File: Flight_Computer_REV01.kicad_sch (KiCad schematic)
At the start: 24 parts, among them J1 Conn_02x03_Counter_Clockwise, J10 Conn_02x16_Top_Bottom, J13 Conn_02x03_Counter_Clockwise, J14 MTR_Signals, J15 Conn_02x30_Odd_Even, J2 Conn_02x03_Counter_Clockwise, J3 AMB POWER, J4 INPUT POWER PASSTHROUGH, J5 Conn_02x16_Top_Bottom, J6 Conn_02x16_Top_Bottom, J7 Conn_02x10_Odd_Even, J8 Conn_02x05_Odd_Even, J9 Conn_02x16_Top_Bottom

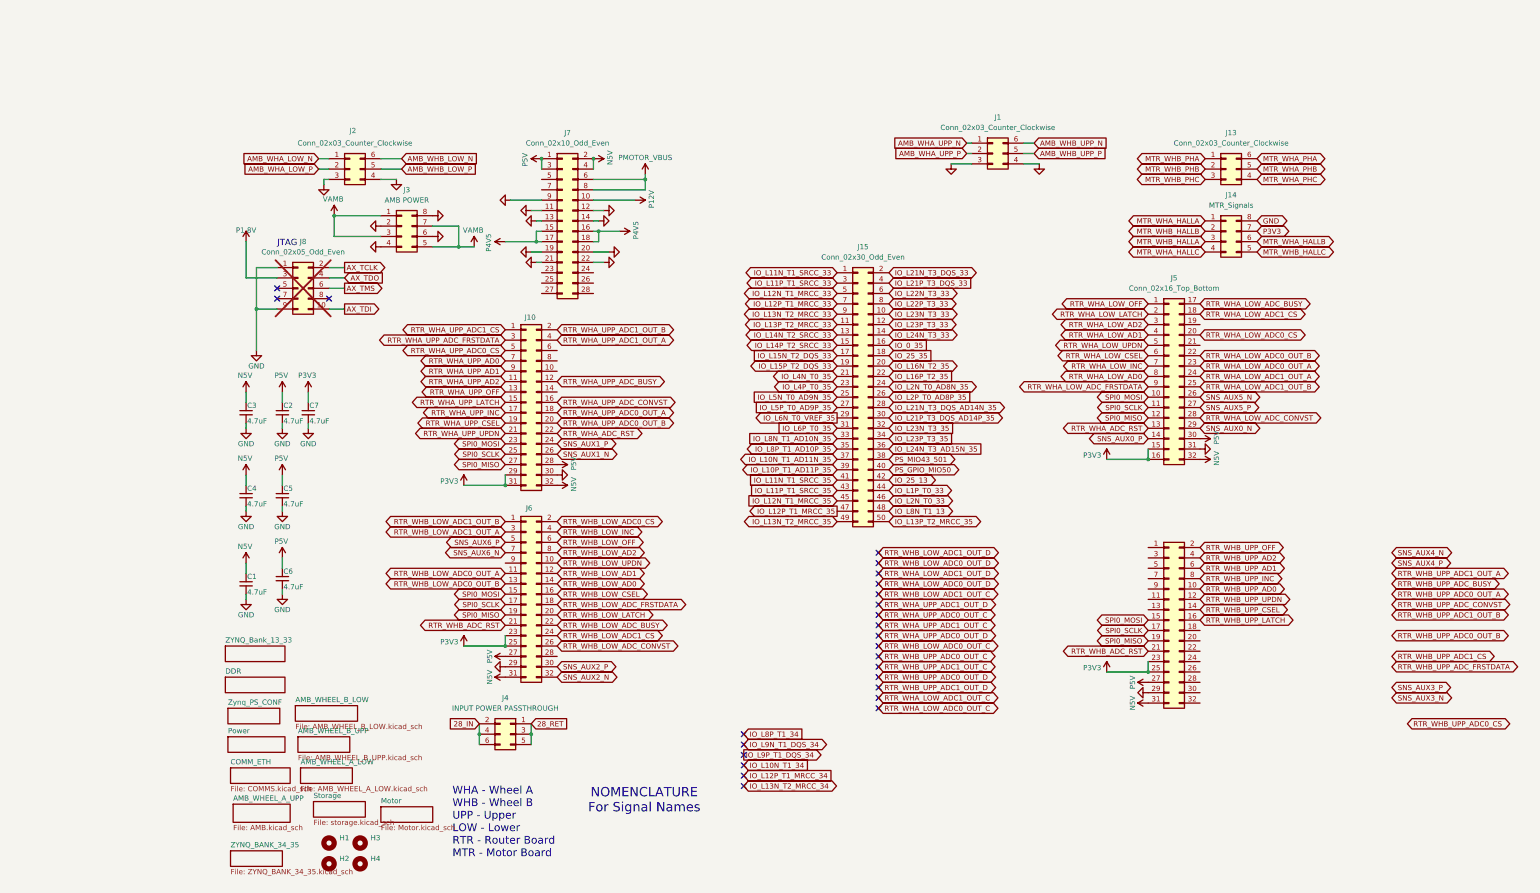
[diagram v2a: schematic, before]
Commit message: Changes to layout pins
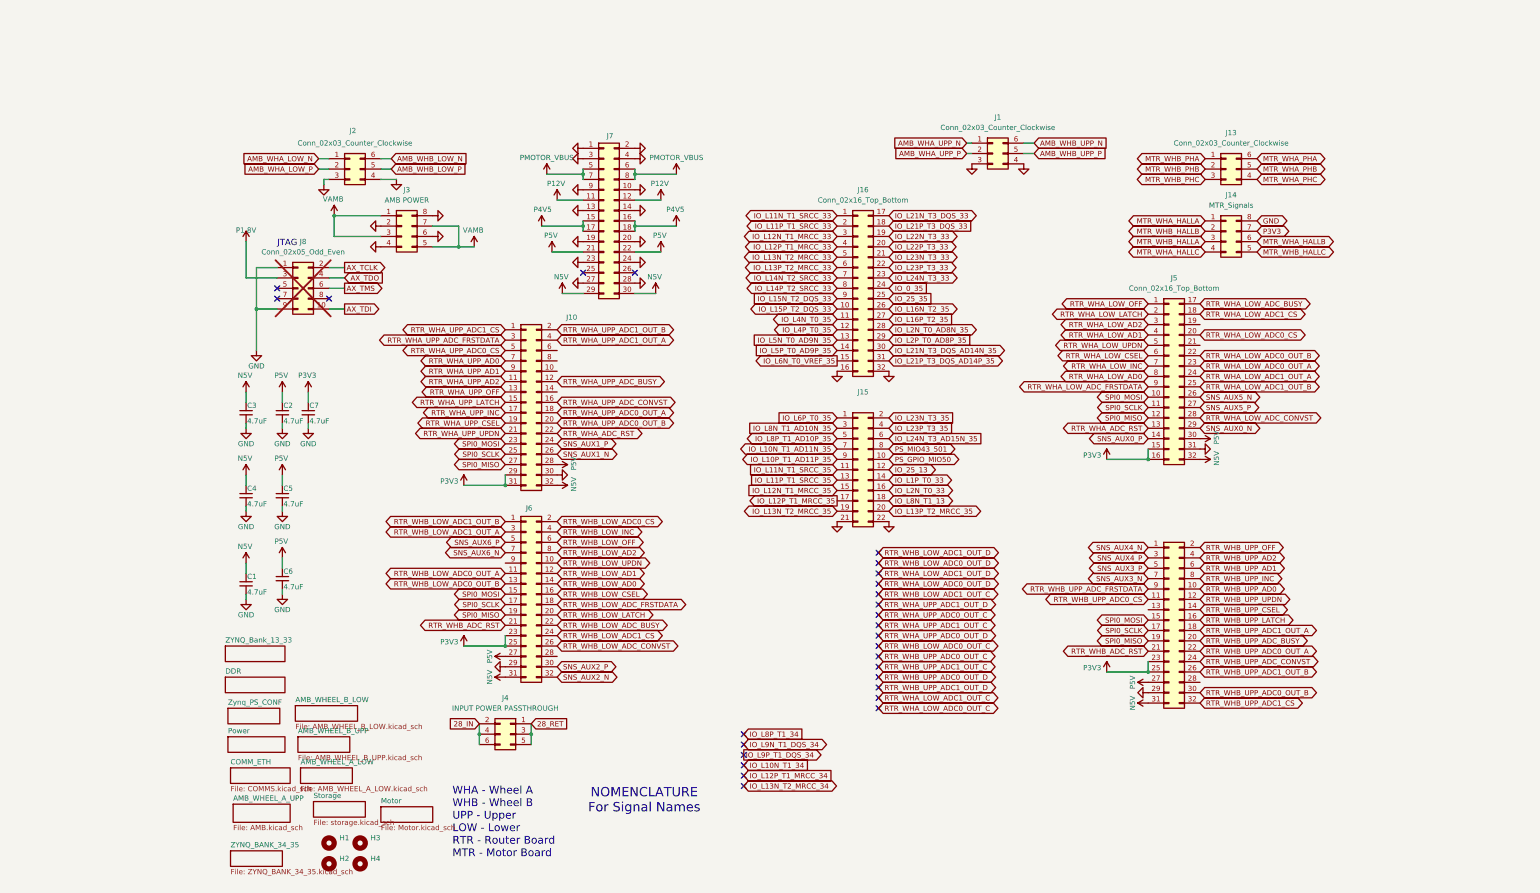
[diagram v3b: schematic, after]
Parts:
- removed J15: Conn_02x30_Odd_Even, Connector_PinHeader_1.27mm:PinHeader_2x25_P1.27mm_Vertical, symbol Connector_Generic:Conn_02x25_Odd_Even
- added J15: Conn_02x30_Odd_Even, Connector_PinHeader_1.27mm:PinHeader_2x11_P1.27mm_Vertical, symbol Connector_Generic:Conn_02x11_Odd_Even
- added J16: Conn_02x16_Top_Bottom, Connector_PinHeader_1.27mm:PinHeader_2x16_P1.27mm_Vertical, symbol Connector_Generic:Conn_02x16_Top_Bottom
- J7: footprint Connector_PinSocket_2.54mm:PinSocket_2x14_P2.54mm_Vertical -> Connector_PinSocket_2.54mm:PinSocket_2x15_P2.54mm_Vertical; symbol Connector_Generic:Conn_02x14_Odd_Even -> Connector_Generic:Conn_02x15_Odd_Even
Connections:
- net GND: now also J7.1 (Pin_1), J7.10 (Pin_10), J7.2 (Pin_2), J7.23 (Pin_23), J7.24 (Pin_24), J7.27 (Pin_27), J7.28 (Pin_28), J7.3 (Pin_3), J7.4 (Pin_4), J15.21 (Pin_21), J15.22 (Pin_22), J16.16 (Pin_16), J16.32 (Pin_32); no longer J7.11 (Pin_11), J7.12 (Pin_12), J7.21 (Pin_21), J7.22 (Pin_22)
- net IO_0_35: now also J16.24 (Pin_24)
- net IO_25_13: now also J15.12 (Pin_12)
- net IO_25_35: now also J16.25 (Pin_25)
- net IO_L10N_T1_AD11N_35: now also J15.7 (Pin_7)
- net IO_L10P_T1_AD11P_35: now also J15.9 (Pin_9)
- net IO_L11N_T1_SRCC_33: now also J16.1 (Pin_1)
- net IO_L11N_T1_SRCC_35: now also J15.11 (Pin_11)
- net IO_L11P_T1_SRCC_33: now also J16.2 (Pin_2)
- net IO_L11P_T1_SRCC_35: now also J15.13 (Pin_13)
- net IO_L12N_T1_MRCC_33: now also J16.3 (Pin_3)
- net IO_L12N_T1_MRCC_35: now also J15.15 (Pin_15)
- net IO_L12P_T1_MRCC_33: now also J16.4 (Pin_4)
- net IO_L12P_T1_MRCC_35: now also J15.17 (Pin_17)
- net IO_L13N_T2_MRCC_33: now also J16.5 (Pin_5)
- net IO_L13N_T2_MRCC_35: now also J15.19 (Pin_19)
- net IO_L13P_T2_MRCC_33: now also J16.6 (Pin_6)
- net IO_L13P_T2_MRCC_35: now also J15.20 (Pin_20)
- net IO_L14N_T2_SRCC_33: now also J16.7 (Pin_7)
- net IO_L14P_T2_SRCC_33: now also J16.8 (Pin_8)
- net IO_L15N_T2_DQS_33: now also J16.9 (Pin_9)
- net IO_L15P_T2_DQS_33: now also J16.10 (Pin_10)
- net IO_L16N_T2_35: now also J16.26 (Pin_26)
- net IO_L16P_T2_35: now also J16.27 (Pin_27)
- net IO_L1P_T0_33: now also J15.14 (Pin_14)
- net IO_L21N_T3_DQS_33: now also J16.17 (Pin_17)
- net IO_L21N_T3_DQS_AD14N_35: now also J16.30 (Pin_30)
- net IO_L21P_T3_DQS_33: now also J16.18 (Pin_18)
- net IO_L21P_T3_DQS_AD14P_35: now also J16.31 (Pin_31)
- net IO_L22N_T3_33: now also J16.19 (Pin_19)
- net IO_L22P_T3_33: now also J16.20 (Pin_20)
- net IO_L23N_T3_33: now also J16.21 (Pin_21)
- net IO_L23N_T3_35: now also J15.2 (Pin_2)
- net IO_L23P_T3_33: now also J16.22 (Pin_22)
- net IO_L23P_T3_35: now also J15.4 (Pin_4)
- net IO_L24N_T3_33: now also J16.23 (Pin_23)
- net IO_L24N_T3_AD15N_35: now also J15.6 (Pin_6)
- net IO_L2N_T0_33: now also J15.16 (Pin_16)
- net IO_L2N_T0_AD8N_35: now also J16.28 (Pin_28)
- net IO_L2P_T0_AD8P_35: now also J16.29 (Pin_29)
- net IO_L4N_T0_35: now also J16.11 (Pin_11)
- net IO_L4P_T0_35: now also J16.12 (Pin_12)
- net IO_L5N_T0_AD9N_35: now also J16.13 (Pin_13)
- net IO_L5P_T0_AD9P_35: now also J16.14 (Pin_14)
- net IO_L6N_T0_VREF_35: now also J16.15 (Pin_15)
- net IO_L6P_T0_35: now also J15.1 (Pin_1)
- net IO_L8N_T1_13: now also J15.18 (Pin_18)
- net IO_L8N_T1_AD10N_35: now also J15.3 (Pin_3)
- net IO_L8P_T1_AD10P_35: now also J15.5 (Pin_5)
- net N5V: now also J7.29 (Pin_29), J7.30 (Pin_30); no longer J7.2 (Pin_2), J7.4 (Pin_4)
- net P12V: now also J7.11 (Pin_11), J7.12 (Pin_12); no longer J7.10 (Pin_10)
- net P5V: now also J7.21 (Pin_21), J7.22 (Pin_22); no longer J7.1 (Pin_1), J7.3 (Pin_3)
- net PMOTOR_VBUS: now also J7.5 (Pin_5), J7.7 (Pin_7)
- net PS_GPIO_MIO50: now also J15.10 (Pin_10)
- net PS_MIO43_501: now also J15.8 (Pin_8)
- net RTR_WHB_UPP_ADC0_CS: now also J9.11 (Pin_11)
- net RTR_WHB_UPP_ADC0_OUT_A: now also J9.22 (Pin_22)
- net RTR_WHB_UPP_ADC0_OUT_B: now also J9.30 (Pin_30)
- net RTR_WHB_UPP_ADC1_CS: now also J9.32 (Pin_32)
- net RTR_WHB_UPP_ADC1_OUT_A: now also J9.18 (Pin_18)
- net RTR_WHB_UPP_ADC1_OUT_B: now also J9.26 (Pin_26)
- net RTR_WHB_UPP_ADC_BUSY: now also J9.20 (Pin_20)
- net RTR_WHB_UPP_ADC_CONVST: now also J9.24 (Pin_24)
- net RTR_WHB_UPP_ADC_FRSTDATA: now also J9.9 (Pin_9)
- net SNS_AUX3_N: now also J9.7 (Pin_7)
- net SNS_AUX3_P: now also J9.5 (Pin_5)
- net SNS_AUX4_N: now also J9.1 (Pin_1)
- net SNS_AUX4_P: now also J9.3 (Pin_3)
- no-connect marks 25 -> 27
